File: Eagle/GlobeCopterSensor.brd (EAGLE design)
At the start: 160 x 100 mm, 11 parts, among them IC1 MS5611-01BA03, U2 ADS1015

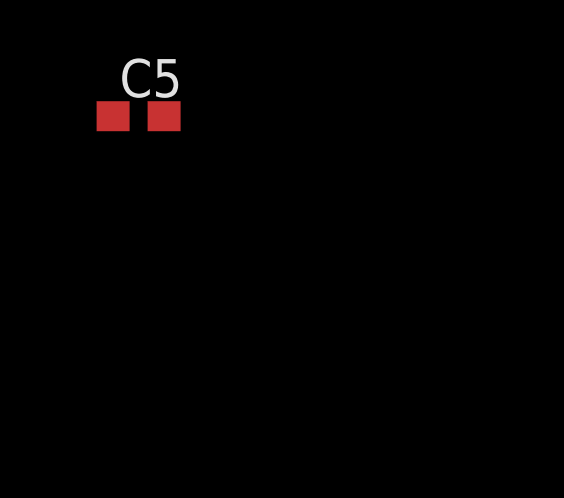
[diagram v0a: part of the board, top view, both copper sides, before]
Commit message: remove unused 3.3v tag, connect rpi gnd, add i2c pullup part
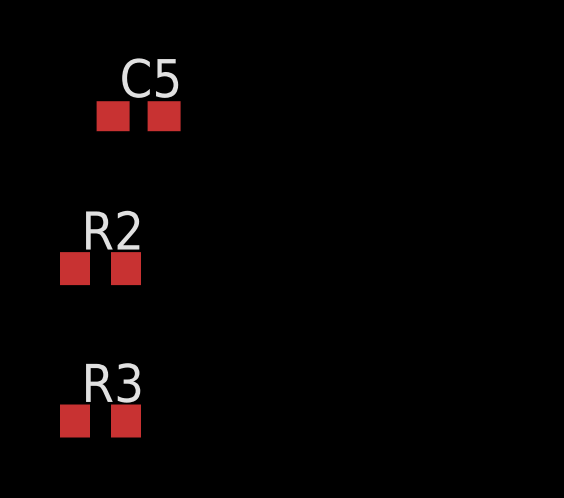
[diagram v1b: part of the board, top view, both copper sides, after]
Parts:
- added R2, R3: 10k, resistor:R0603
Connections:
- removed net 3V3@1: U$2.1
- net 3V3_LDO: now also R2.2, R3.2
- net GND: now also U$2.39
- net I2C_SCL: now also R3.1
- net I2C_SDA: now also R2.1
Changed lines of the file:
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@@
 <element name="C4" library="resistor" library_urn="urn:adsk.eagle:library:348" package="C0603" value="0u1" x="-33.02" y="-33.02"/>
 <element name="C5" library="resistor" library_urn="urn:adsk.eagle:library:348" package="C0603" value="10n" x="-33.02" y="-38.1"/>
+<element name="R2" library="resistor" library_urn="urn:adsk.eagle:library:348" package="R0603" value="10k" x="-34.29" y="-43.18"/>
+<element name="R3" library="resistor" library_urn="urn:adsk.eagle:library:348" package="R0603" value="10k" x="-34.29" y="-48.26"/>
 </elements>
 <signals>
@@
 <contactref element="C5" pad="2"/>
 <contactref element="U$1" pad="9"/>
-<wire x1="-32.17" y1="-33.02" x2="-32.17" y2="-38.1" width="0" layer="19" extent="1-1"/>
-<wire x1="-32.17" y1="-27.94" x2="-32.17" y2="-33.02" width="0" layer="19" extent="1-1"/>
-<wire x1="-32.17" y1="-22.86" x2="-32.17" y2="-27.94" width="0" layer="19" extent="1-1"/>
-<wire x1="-32.17" y1="-17.78" x2="-32.17" y2="-22.86" width="0" layer="19" extent="1-1"/>
-<wire x1="-34.13" y1="1.94" x2="-32.17" y2="-17.78" width="0" layer="19" extent="1-1"/>
-<wire x1="-27.67" y1="1.76" x2="-34.13" y2="1.94" width="0" layer="19" extent="1-1"/>
-<wire x1="-26.67" y1="1.76" x2="-27.67" y2="1.76" width="0" layer="19" extent="1-1"/>
-<wire x1="-22.005" y1="0.8922" x2="-26.67" y2="1.76" width="0" layer="19" extent="1-1"/>
-<wire x1="-21.355" y1="0.8922" x2="-22.005" y2="0.8922" width="0" layer="19" extent="1-1"/>
-<wire x1="-20.705" y1="0.8922" x2="-21.355" y2="0.8922" width="0" layer="19" extent="1-1"/>
-<wire x1="-20.055" y1="0.8922" x2="-20.705" y2="0.8922" width="0" layer="19" extent="1-1"/>
-<wire x1="-19.405" y1="0.8922" x2="-20.055" y2="0.8922" width="0" layer="19" extent="1-1"/>
+<contactref element="U$2" pad="39"/>
+<wire x1="13.13" y1="13.7" x2="56.63" y2="25.23" width="0" layer="19" extent="1-1"/>
+<wire x1="12.03" y1="14.4" x2="13.13" y2="13.7" width="0" layer="19" extent="1-1"/>
+<wire x1="11.23" y1="11" x2="13.13" y2="13.7" width="0" layer="19" extent="1-1"/>
+<wire x1="-13.555" y1="0.8922" x2="11.23" y2="11" width="0" layer="19" extent="1-1"/>
+<wire x1="-19.405" y1="0.8922" x2="-13.555" y2="0.8922" width="0" layer="19" extent="1-1"/>
+<wire x1="-20.055" y1="0.8922" x2="-19.405" y2="0.8922" width="0" layer="19" extent="1-1"/>
+<wire x1="-20.705" y1="0.8922" x2="-20.055" y2="0.8922" width="0" layer="19" extent="1-1"/>
+<wire x1="-21.355" y1="0.8922" x2="-20.705" y2="0.8922" width="0" layer="19" extent="1-1"/>
+<wire x1="-22.005" y1="0.8922" x2="-21.355" y2="0.8922" width="0" layer="19" extent="1-1"/>
+<wire x1="-26.67" y1="1.76" x2="-22.005" y2="0.8922" width="0" layer="19" extent="1-1"/>
+<wire x1="-27.67" y1="1.76" x2="-26.67" y2="1.76" width="0" layer="19" extent="1-1"/>
 <wire x1="-19.405" y1="6.7278" x2="-19.405" y2="0.8922" width="0" layer="19" extent="1-1"/>
-<wire x1="-13.555" y1="0.8922" x2="-19.405" y2="0.8922" width="0" layer="19" extent="1-1"/>
-<wire x1="11.23" y1="11" x2="-13.555" y2="0.8922" width="0" layer="19" extent="1-1"/>
-<wire x1="13.13" y1="13.7" x2="11.23" y2="11" width="0" layer="19" extent="1-1"/>
-<wire x1="12.03" y1="14.4" x2="13.13" y2="13.7" width="0" layer="19" extent="1-1"/>
+<wire x1="-34.13" y1="1.94" x2="-27.67" y2="1.76" width="0" layer="19" extent="1-1"/>
+<wire x1="-32.17" y1="-17.78" x2="-34.13" y2="1.94" width="0" layer="19" extent="1-1"/>
+<wire x1="-32.17" y1="-22.86" x2="-32.17" y2="-17.78" width="0" layer="19" extent="1-1"/>
+<wire x1="-32.17" y1="-27.94" x2="-32.17" y2="-22.86" width="0" layer="19" extent="1-1"/>
+<wire x1="-32.17" y1="-33.02" x2="-32.17" y2="-27.94" width="0" layer="19" extent="1-1"/>
+<wire x1="-32.17" y1="-38.1" x2="-32.17" y2="-33.02" width="0" layer="19" extent="1-1"/>
 </signal>
 <signal name="I2C_SDA">
@@
 <contactref element="IC1" pad="P$7"/>
 <contactref element="U$1" pad="24"/>
-<wire x1="10.43" y1="14.4" x2="10.91" y2="25.23" width="0" layer="19" extent="1-1"/>
-<wire x1="-21.355" y1="6.7278" x2="10.43" y2="14.4" width="0" layer="19" extent="1-1"/>
-<wire x1="-27.17" y1="5.86" x2="-21.355" y2="6.7278" width="0" layer="19" extent="1-1"/>
-<wire x1="-31.92" y1="3.14" x2="-27.17" y2="5.86" width="0" layer="19" extent="1-1"/>
+<contactref element="R2" pad="1"/>
+<wire x1="-31.92" y1="3.14" x2="-35.14" y2="-43.18" width="0" layer="19" extent="1-1"/>
+<wire x1="-27.17" y1="5.86" x2="-31.92" y2="3.14" width="0" layer="19" extent="1-1"/>
+<wire x1="-21.355" y1="6.7278" x2="-27.17" y2="5.86" width="0" layer="19" extent="1-1"/>
+<wire x1="10.43" y1="14.4" x2="-21.355" y2="6.7278" width="0" layer="19" extent="1-1"/>
+<wire x1="10.91" y1="25.23" x2="10.43" y2="14.4" width="0" layer="19" extent="1-1"/>
 </signal>
 <signal name="I2C_SCL">
@@
 <contactref element="IC1" pad="P$8"/>
 <contactref element="U$1" pad="23"/>
-<wire x1="10.83" y1="14.4" x2="13.45" y2="25.23" width="0" layer="19" extent="1-1"/>
-<wire x1="-20.705" y1="6.7278" x2="10.83" y2="14.4" width="0" layer="19" extent="1-1"/>
-<wire x1="-27.67" y1="5.86" x2="-20.705" y2="6.7278" width="0" layer="19" extent="1-1"/>
-<wire x1="-31.92" y1="4.44" x2="-27.67" y2="5.86" width="0" layer="19" extent="1-1"/>
-</signal>
-<signal name="3V3@1">
-<contactref element="U$2" pad="1"/>
+<contactref element="R3" pad="1"/>
+<wire x1="-31.92" y1="4.44" x2="-35.14" y2="-48.26" width="0" layer="19" extent="1-1"/>
+<wire x1="-27.67" y1="5.86" x2="-31.92" y2="4.44" width="0" layer="19" extent="1-1"/>
+<wire x1="-20.705" y1="6.7278" x2="-27.67" y2="5.86" width="0" layer="19" extent="1-1"/>
+<wire x1="10.83" y1="14.4" x2="-20.705" y2="6.7278" width="0" layer="19" extent="1-1"/>
+<wire x1="13.45" y1="25.23" x2="10.83" y2="14.4" width="0" layer="19" extent="1-1"/>
 </signal>
 <signal name="3V3_LDO">
@@
 <contactref element="U$1" pad="8"/>
 <contactref element="C5" pad="1"/>
+<contactref element="R2" pad="2"/>
+<contactref element="R3" pad="2"/>
+<wire x1="-33.44" y1="-43.18" x2="-33.44" y2="-48.26" width="0" layer="19" extent="1-1"/>
+<wire x1="-33.87" y1="-38.1" x2="-33.44" y2="-43.18" width="0" layer="19" extent="1-1"/>
 <wire x1="-33.87" y1="-27.94" x2="-33.87" y2="-38.1" width="0" layer="19" extent="1-1"/>
 <wire x1="-33.87" y1="-22.86" x2="-33.87" y2="-27.94" width="0" layer="19" extent="1-1"/>

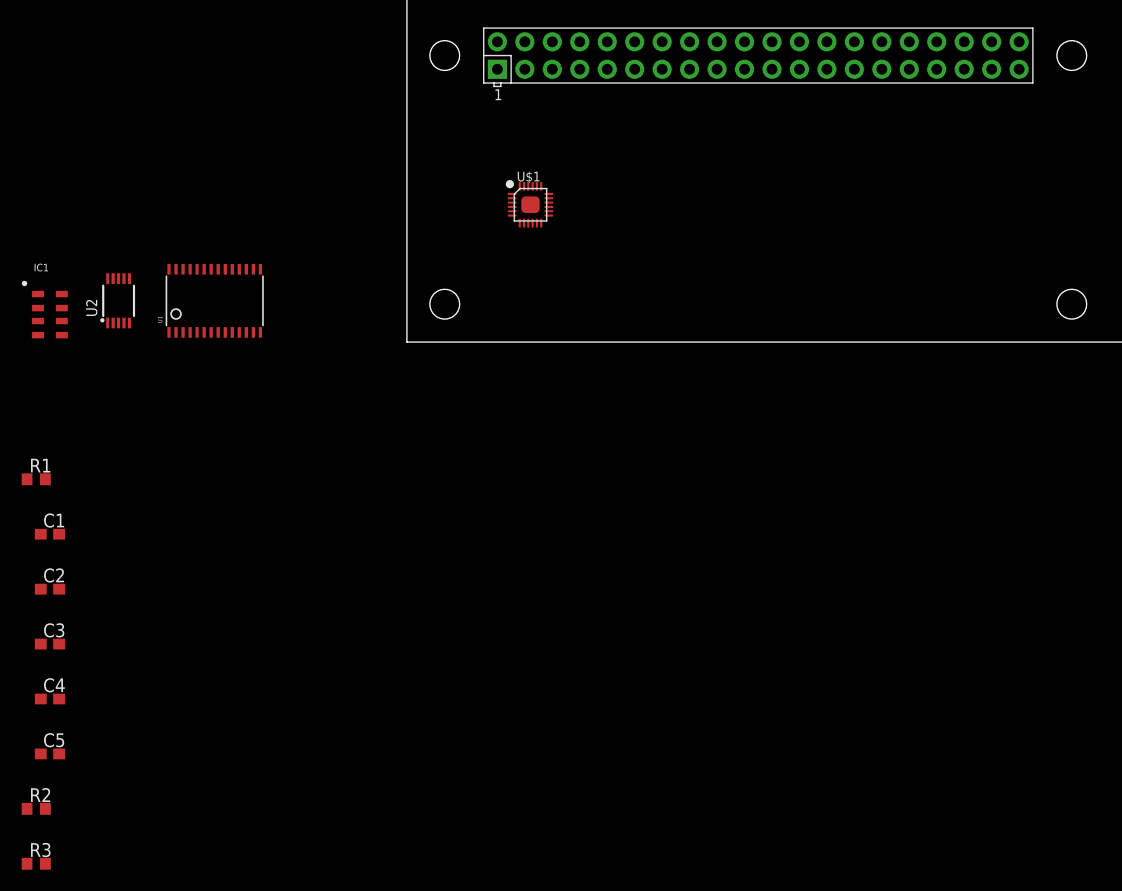
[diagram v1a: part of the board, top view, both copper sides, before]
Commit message: センサー部の基本的な設計完了　電源部等細部要調整
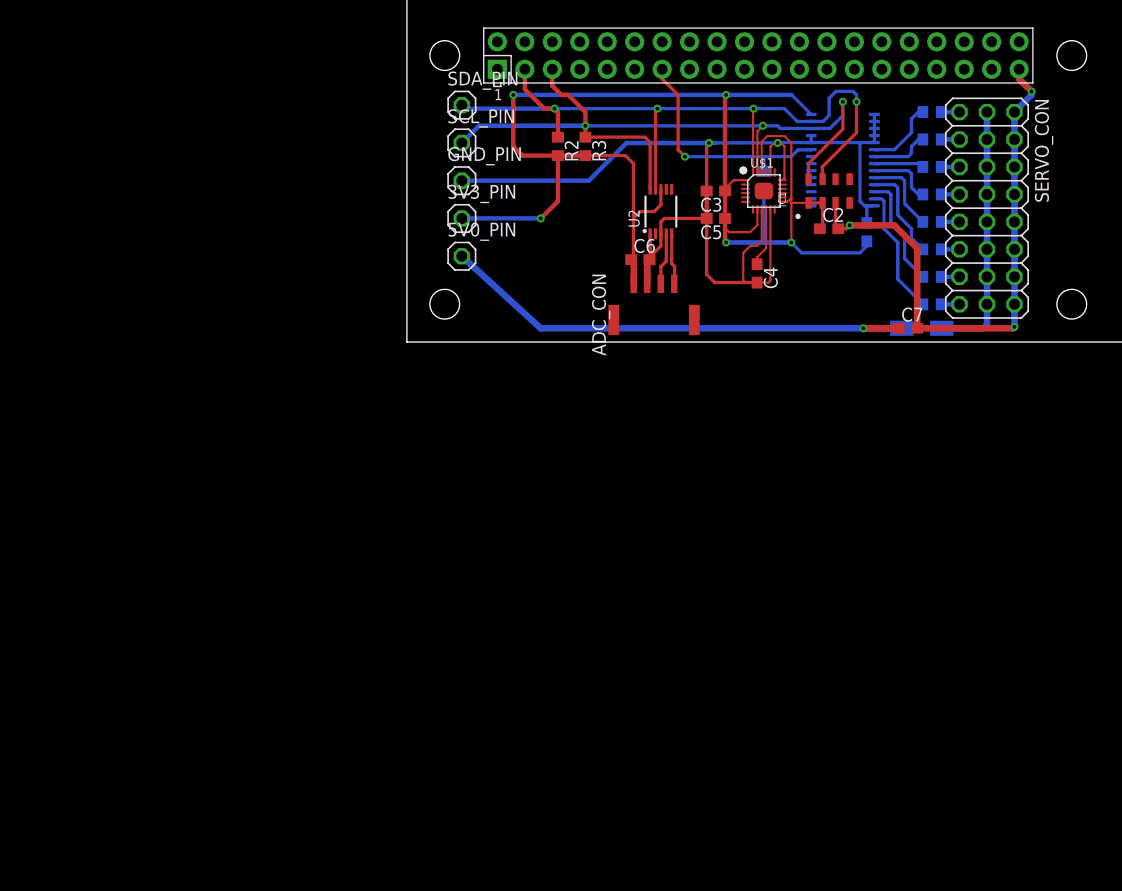
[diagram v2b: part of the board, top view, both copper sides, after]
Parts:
- added 3V3_PIN, 5V0_PIN, GND_PIN, SCL_PIN, SDA_PIN: (no value), pinhead:1X01
- added ADC_CON: BM04B-GHS-TBT, connector:BM04B-GHS-TBT
- added C6, C7: 0u1, resistor:C0603
- added F1: 1206L, ptc-littlefuse:1206L
- added R10, R11, R4, R5, R6, R7, R8, R9: 220, resistor:R0603
- added SERVO_CON: PINHD-3X8, pinhead:3X8
- C4: value 0u1 -> 2u2
- moved R3 83.6 mm to (16.5, 18.1), turned to 270 degrees
- moved C1 80.6 mm to (42.5, 10.2), flipped to the bottom, turned to 90 degrees
- moved C2 79.4 mm to (39.1, 10.5)
- moved C5 79.0 mm to (28.6, 11.4), turned to 180 degrees
- moved R2 78.0 mm to (14.0, 18.1), turned to 270 degrees
- moved C4 76.3 mm to (32.4, 6.35), turned to 270 degrees
- moved C3 74.5 mm to (28.6, 14.0), turned to 180 degrees
- moved IC1 73.0 mm to (39.1, 14.0), turned to 90 degrees
- moved R1 72.8 mm to (33.0, 14.9), flipped to the bottom, turned to 270 degrees
- moved U1 59.5 mm to (40.3, 16.8), flipped to the bottom, turned to 270 degrees
- moved U2 50.8 mm to (23.5, 12.1)
- moved U$1 21.6 mm to (33.0, 14.0)
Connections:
- removed net N$1: R1.1, U1.23
- new net !LED_AMBER!: U$2.18
- new net !LED_BLUE!: U$2.22
- new net 5V0: 5V0_PIN.1, C7.1, F1.P$1
- new net ADC0_IN: ADC_CON.3, U2.4
- new net ADC1_IN: ADC_CON.4, U2.5
- new net MPU9250_DRDY: U$1.12
- new net MPU925_DRDY: U$2.16
- new net N$3: F1.P$2, SERVO_CON.11, SERVO_CON.14, SERVO_CON.17, SERVO_CON.2, SERVO_CON.20, SERVO_CON.23, SERVO_CON.5, SERVO_CON.8
- new net PWM0_CON: R4.2, SERVO_CON.1
- new net PWM0_OUT: R4.1, U1.6
- new net PWM1_CON: R5.2, SERVO_CON.4
- new net PWM1_OUT: R5.1, U1.7
- new net PWM2_CON: R6.2, SERVO_CON.7
- new net PWM2_OUT: R6.1, U1.8
- new net PWM3_CON: R7.2, SERVO_CON.10
- new net PWM3_OUT: R7.1, U1.9
- new net PWM4_CON: R8.2, SERVO_CON.13
- new net PWM4_OUT: R8.1, U1.10
- new net PWM5_CON: R9.2, SERVO_CON.16
- new net PWM5_OUT: R9.1, U1.11
- new net PWM6_CON: R10.2, SERVO_CON.19
- new net PWM6_OUT: R10.1, U1.12
- new net PWM7_CON: R11.2, SERVO_CON.22
- new net PWM7_OUT: R11.1, U1.13
- net 3V3_LDO: now also 3V3_PIN.1, ADC_CON.1, C6.1, U$1.1
- net GND: now also ADC_CON.2, C6.2, C7.2, GND_PIN.1, SERVO_CON.12, SERVO_CON.15, SERVO_CON.18, SERVO_CON.21, SERVO_CON.24, SERVO_CON.3, SERVO_CON.6, SERVO_CON.9, U$1.11, U1.25
- net I2C_SCL: now also SCL_PIN.1
- net I2C_SDA: now also SDA_PIN.1
- net PWM_EN: now also R1.1, U1.23
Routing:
- net GND: track 0.00 -> 160.5 mm, vias 0 -> 5
- net 3V3_LDO: track 0.00 -> 137.0 mm, vias 0 -> 5
- net I2C_SDA: track 0.00 -> 70.1 mm, vias 0 -> 4
- net I2C_SCL: track 0.00 -> 69.4 mm, vias 0 -> 3
- net 5V0: track 0.00 -> 46.6 mm, vias 0 -> 1
- net N$3: track 0.00 -> 24.0 mm
- net PWM_EN: track 0.00 -> 22.3 mm, vias 0 -> 1
- net PWM7_OUT: track 0.00 -> 12.0 mm
- net PWM6_OUT: track 0.00 -> 10.5 mm
- net PWM5_OUT: track 0.00 -> 8.95 mm
- net PWM4_OUT: track 0.00 -> 7.42 mm
- net PWM0_OUT: track 0.00 -> 6.67 mm
- net PWM3_OUT: track 0.00 -> 6.14 mm
- net PWM1_OUT: track 0.00 -> 5.51 mm
- net N$2: track 0.00 -> 5.42 mm
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
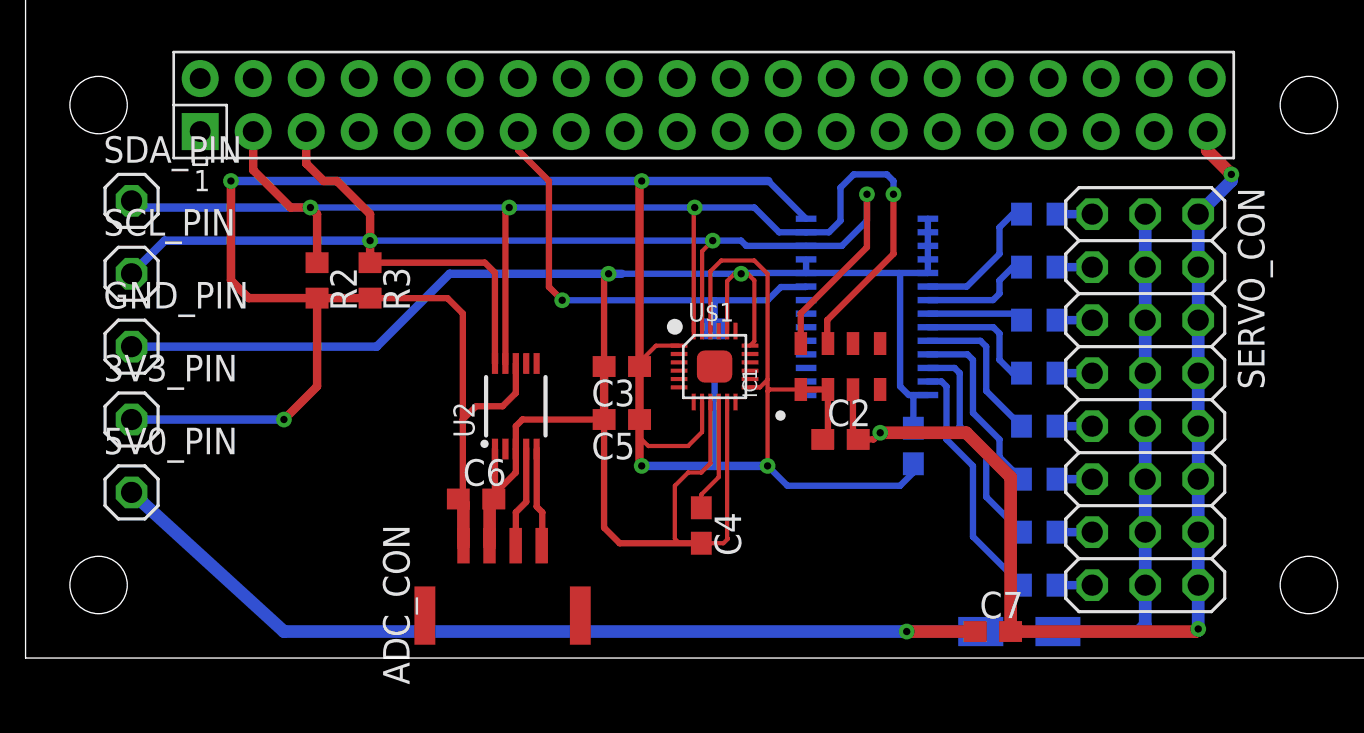
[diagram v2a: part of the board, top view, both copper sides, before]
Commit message: 部品をすべて部品面に移動
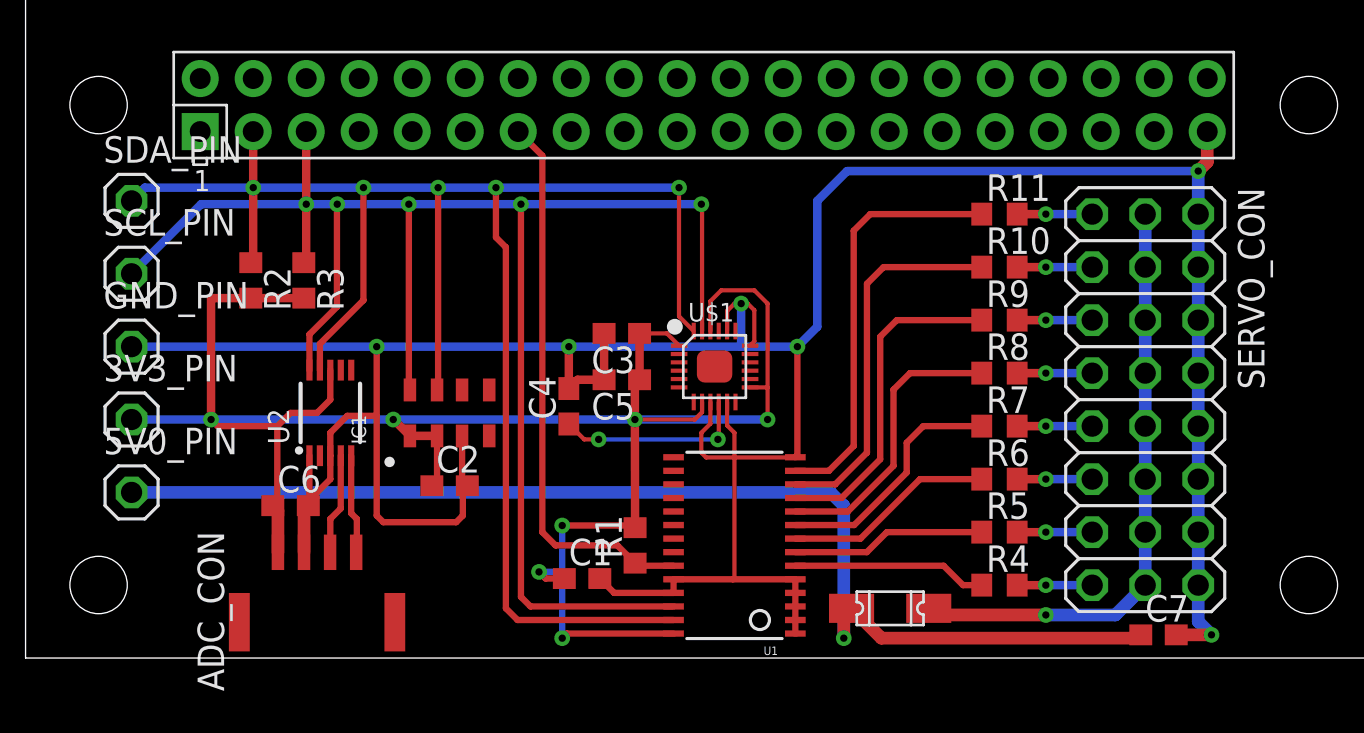
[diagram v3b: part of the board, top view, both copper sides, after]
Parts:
- moved C2 18.9 mm to (20.3, 8.26)
- moved IC1 18.9 mm to (20.3, 11.7)
- moved R11 17.9 mm to (46.7, 21.3), flipped to the top, turned to 0 degrees
- moved R4 17.9 mm to (46.7, 3.49), flipped to the top, turned to 0 degrees
- moved C1 17.1 mm to (26.7, 3.81), flipped to the top, turned to 0 degrees
- moved U1 13.1 mm to (34.0, 5.40), flipped to the top, turned to 90 degrees
- moved R10 12.8 mm to (46.7, 18.7), flipped to the top, turned to 0 degrees
- moved R5 12.8 mm to (46.7, 6.03), flipped to the top, turned to 0 degrees
- moved R1 10.3 mm to (29.2, 5.40), flipped to the top, turned to 90 degrees
- moved C6 8.90 mm to (12.7, 7.30)
- moved U2 8.90 mm to (14.6, 11.7)
- moved ADC_CON 8.90 mm to (14.0, 2.86)
- moved C4 8.54 mm to (26.0, 12.1), turned to 90 degrees
- moved C7 7.94 mm to (54.3, 1.11)
- moved R6 7.85 mm to (46.7, 8.57), flipped to the top, turned to 0 degrees
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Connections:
- net PWM0_CON: now also SERVO_CON.22; no longer SERVO_CON.1
- net PWM1_CON: now also SERVO_CON.19; no longer SERVO_CON.4
- net PWM2_CON: now also SERVO_CON.16; no longer SERVO_CON.7
- net PWM3_CON: now also SERVO_CON.13; no longer SERVO_CON.10
- net PWM4_CON: now also SERVO_CON.10; no longer SERVO_CON.13
- net PWM5_CON: now also SERVO_CON.7; no longer SERVO_CON.16
- net PWM6_CON: now also SERVO_CON.4; no longer SERVO_CON.19
- net PWM7_CON: now also SERVO_CON.1; no longer SERVO_CON.22
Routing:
- net 3V3_LDO: track 137.0 -> 103.6 mm, vias 5 -> 7
- net I2C_SDA: track 70.1 -> 87.9 mm, vias 4 -> 5
- net I2C_SCL: track 69.4 -> 84.9 mm, vias 3 -> 5
- net 5V0: track 46.6 -> 56.8 mm
- net PWM7_OUT: track 12.0 -> 20.1 mm
- net PWM6_OUT: track 10.5 -> 18.0 mm
- net PWM5_OUT: track 8.95 -> 15.9 mm
- net PWM4_OUT: track 7.42 -> 13.8 mm
- net PWM3_OUT: track 6.14 -> 11.7 mm
- net PWM2_OUT: track 4.62 -> 10.1 mm
- net N$3: track 24.0 -> 28.9 mm, vias 0 -> 1
- net PWM_EN: track 22.3 -> 26.6 mm, vias 1 -> 0
- net N$2: track 5.42 -> 9.28 mm, vias 0 -> 2
- net PWM1_OUT: track 5.51 -> 9.33 mm
- net PWM0_OUT: track 6.67 -> 9.32 mm
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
